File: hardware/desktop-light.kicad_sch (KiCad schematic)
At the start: 54 parts

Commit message: led position
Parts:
- added D55, D56, D57, D58, D59, D60: WS2812B, LED_SMD:LED_WS2812B_PLCC4_5.0x5.0mm_P3.2mm, symbol LED:WS2812B
- added J1, J2: Conn_01x06, Connector_JST:JST_SH_BM06B-SRSS-TB_1x06-1MP_P1.00mm_Vertical, symbol Connector_Generic:Conn_01x06
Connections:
- net +5V: now also D55.1 (VDD), D56.1 (VDD), D57.1 (VDD), D58.1 (VDD), D59.1 (VDD), D60.1 (VDD), J1.1 (Pin_1), J1.2 (Pin_2), J2.5 (Pin_5), J2.6 (Pin_6)
- net GND: now also D55.3 (VSS), D56.3 (VSS), D57.3 (VSS), D58.3 (VSS), D59.3 (VSS), D60.3 (VSS), J1.5 (Pin_5), J1.6 (Pin_6), J2.1 (Pin_1), J2.2 (Pin_2)
- net at D54.2 (DOUT): now also D55.4 (DIN)
- net at D1.4 (DIN): now also J1.3 (Pin_3)
- new net: D55.2 (DOUT), D56.4 (DIN)
- new net: D59.2 (DOUT), D60.4 (DIN)
- new net: D58.2 (DOUT), D59.4 (DIN)
- new net: D56.2 (DOUT), D57.4 (DIN)
- new net: D57.2 (DOUT), D58.4 (DIN)
- new net DIN: J2.4 (Pin_4)
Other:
- moved on the sheet: D1, D10, D11, D12, D13, D14, D15, D16, D17, D18, D19, D2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

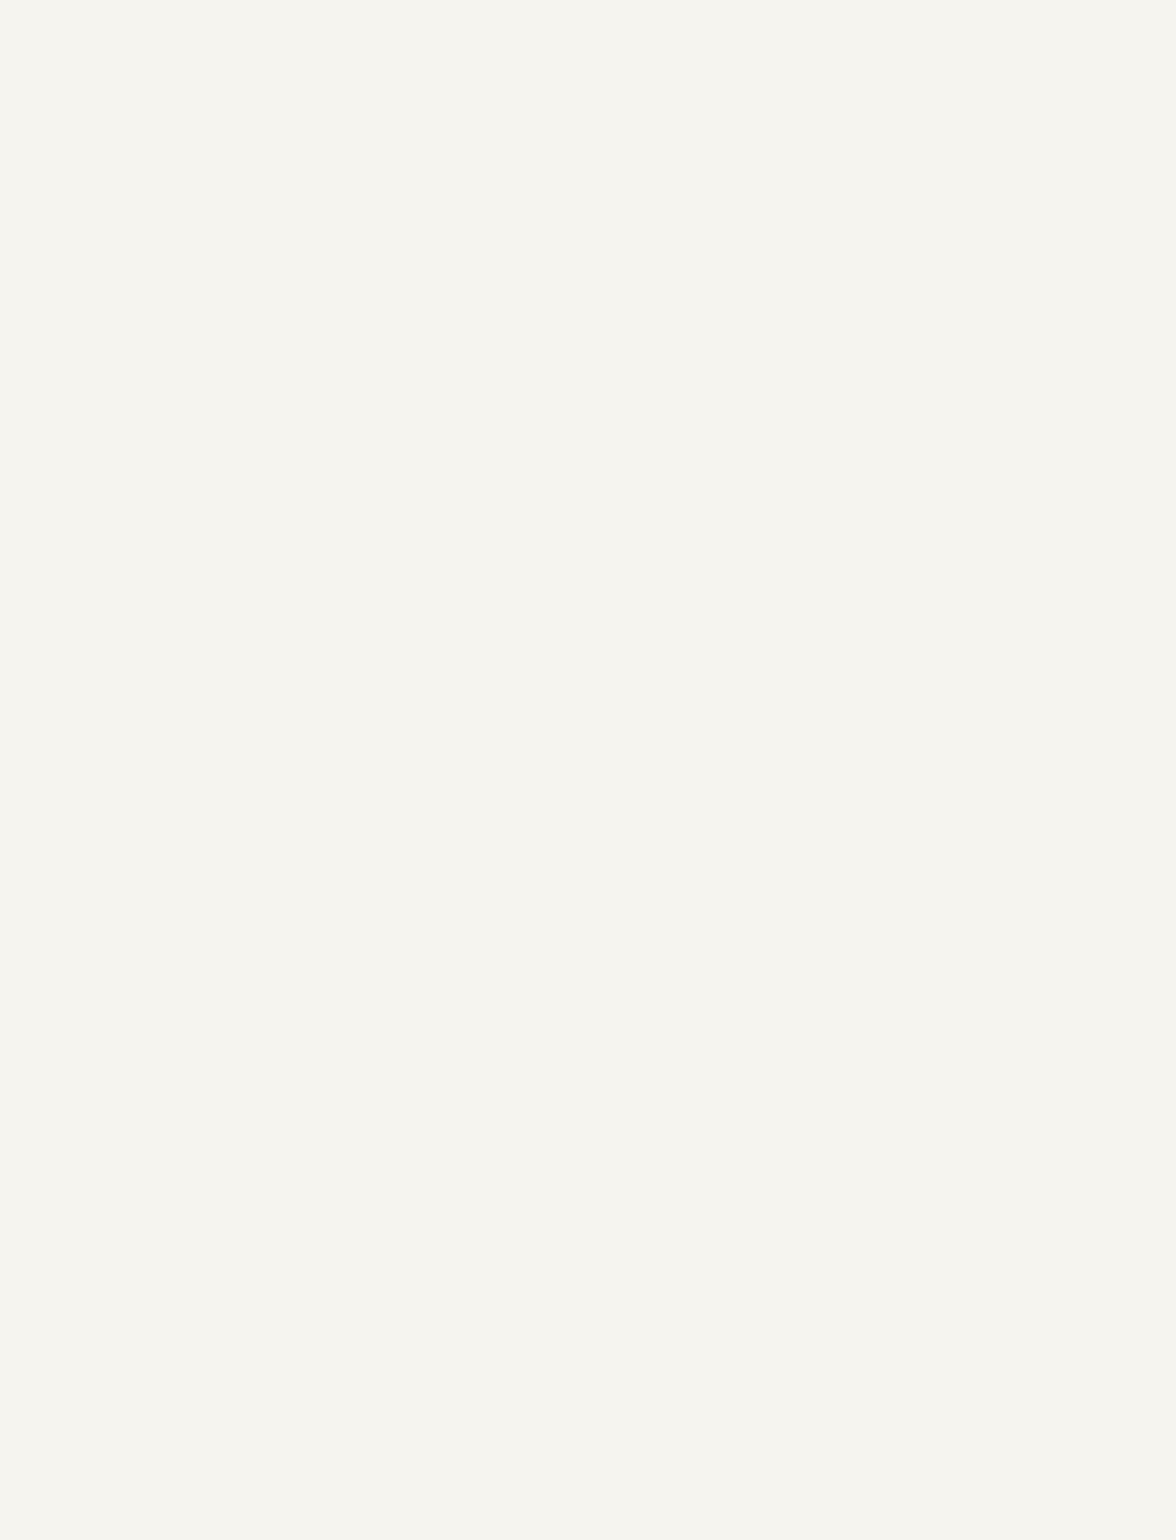
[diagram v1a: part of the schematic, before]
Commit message: add esp32
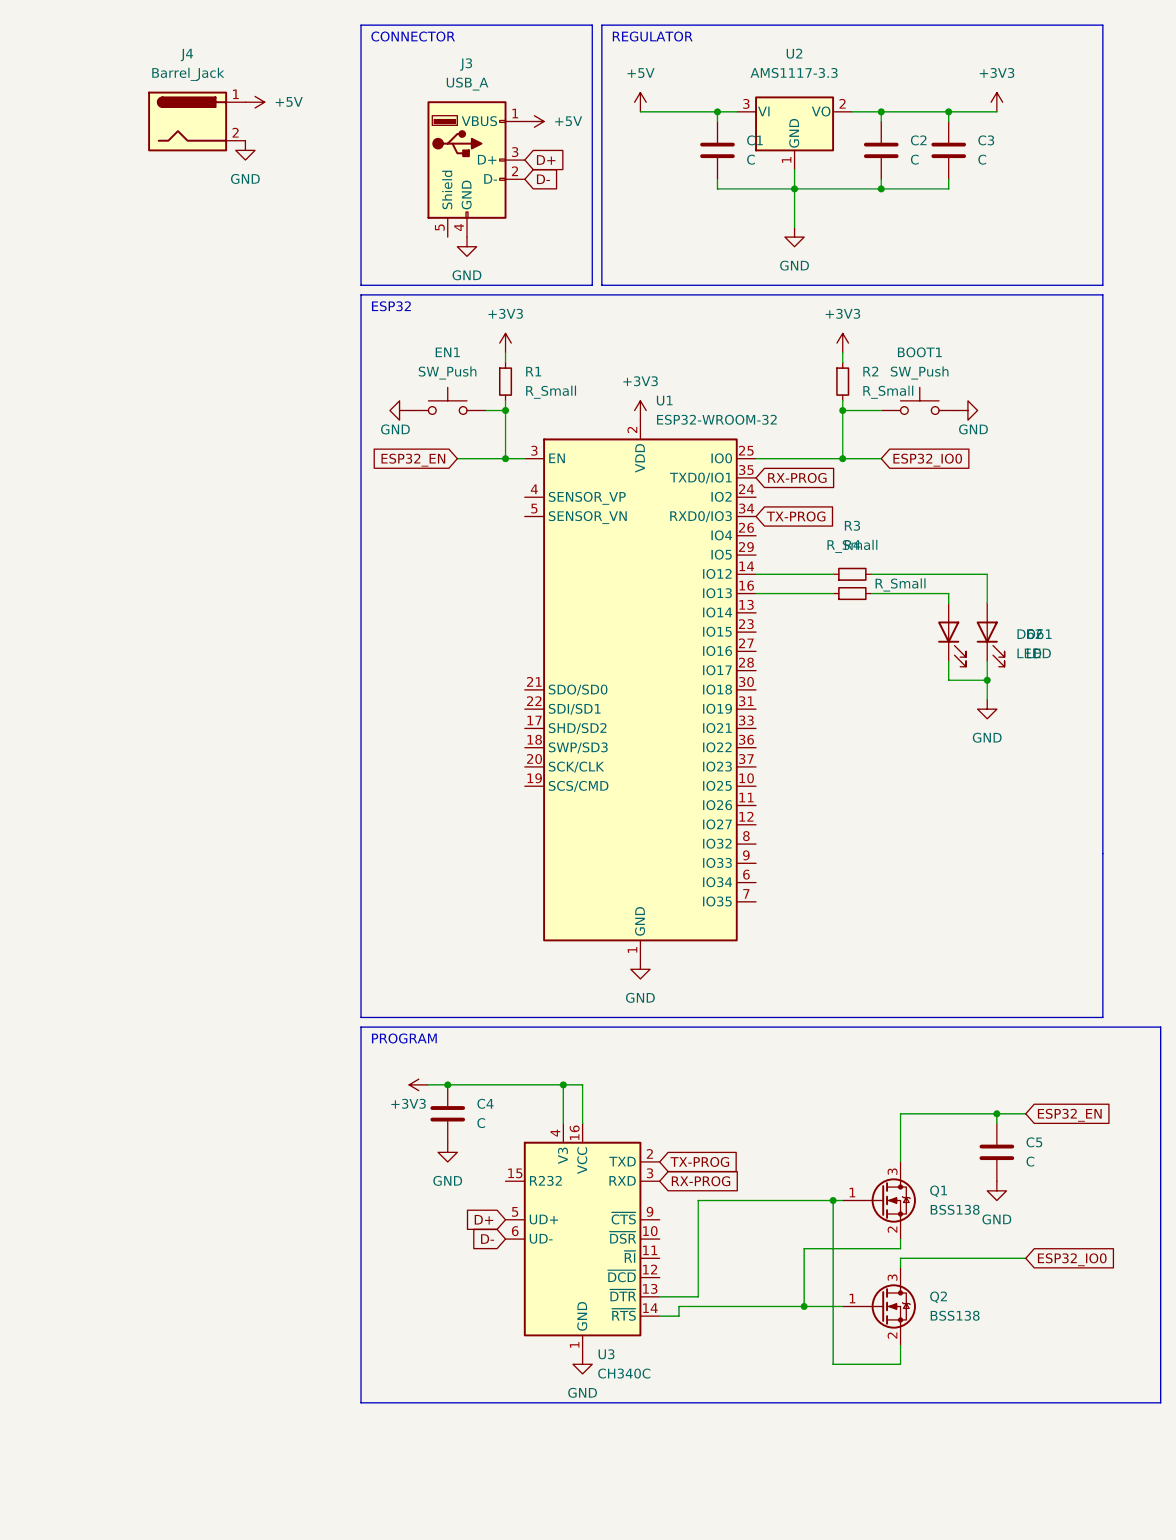
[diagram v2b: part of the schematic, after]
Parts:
- added BOOT1, EN1: SW_Push, Button_Switch_SMD:SW_SPST_FSMSM, symbol Switch:SW_Push
- added C1, C2, C3, C4, C5: C, Capacitor_SMD:C_0603_1608Metric, symbol Device:C
- added D61, D62: LED, LED_SMD:LED_0603_1608Metric, symbol Device:LED
- added J3: USB_A, Connector_USB:USB_A_CNCTech_1001-011-01101_Horizontal, symbol Connector:USB_A
- added J4: Barrel_Jack, symbol Connector:Barrel_Jack
- added Q1, Q2: BSS138, Package_TO_SOT_SMD:SOT-23, symbol Transistor_FET:BSS138
- added R1, R2, R3, R4: R_Small, Resistor_SMD:R_0603_1608Metric, symbol Device:R_Small
- added U1: ESP32-WROOM-32, RF_Module:ESP32-WROOM-32, symbol RF_Module:ESP32-WROOM-32
- added U2: AMS1117-3.3, Package_TO_SOT_SMD:SOT-223-3_TabPin2, symbol Regulator_Linear:AMS1117-3.3
- added U3: CH340C, Package_SO:SOIC-16_3.9x9.9mm_P1.27mm, symbol Interface_USB:CH340C
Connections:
- net +5V: now also C1.1, J3.1 (VBUS), J4.1, U2.3 (VI)
- net GND: now also BOOT1.2, C1.2, C2.2, C3.2, C4.2, C5.2, D61.1 (K), D62.1 (K), EN1.1, J3.4 (GND), J4.2, U1.1 (GND), U1.15 (GND), U1.38 (GND), U1.39 (GND), U2.1 (GND), U3.1 (GND)
- new net: Q1.1 (G), Q2.2 (S), U3.13 (~{DTR})
- new net: Q1.2 (S), Q2.1 (G), U3.14 (~{RTS})
- new net: R4.1, U1.16 (IO13)
- new net: D61.2 (A), R4.2
- new net: R3.1, U1.14 (IO12)
- new net: D62.2 (A), R3.2
- new net +3V3: C2.1, C3.1, C4.1, R1.1, R2.1, U1.2 (VDD), U2.2 (VO), U3.16 (VCC), U3.4 (V3)
- new net D+: J3.3 (D+), U3.5 (UD+)
- new net D-: J3.2 (D-), U3.6 (UD-)
- new net ESP32_EN: C5.1, EN1.2, Q1.3 (D), R1.2, U1.3 (EN)
- new net ESP32_IO0: BOOT1.1, Q2.3 (D), R2.2, U1.25 (IO0)
- new net RX-PROG: U1.35 (TXD0/IO1), U3.3 (RXD)
- new net TX-PROG: U1.34 (RXD0/IO3), U3.2 (TXD)
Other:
- note added: "CONNECTOR"
- note added: "ESP32"
- note added: "PROGRAM"
- note added: "REGULATOR"

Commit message: add clock
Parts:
- removed J3: USB_A, Connector_USB:USB_A_CNCTech_1001-011-01101_Horizontal, symbol Connector:USB_A
- added BT1: Battery_Cell, Battery:BatteryHolder_LINX_BAT-HLD-012-SMT, symbol Device:Battery_Cell
- added BTN1, BTN2, BTN3: SW_Push, Button_Switch_SMD:SW_SPST_FSMSM, symbol Switch:SW_Push
- added C6: C_Small, Capacitor_SMD:C_0603_1608Metric, symbol Device:C_Small
- added J3: USB_B_Micro, Connector_USB:USB_Micro-B_Molex-105017-0001, symbol Connector:USB_B_Micro
- added R5, R6, R7, R8, R9: R_Small, Resistor_SMD:R_0603_1608Metric, symbol Device:R_Small
- added U4: PCF8523T, Package_SO:SOIC-8_3.9x4.9mm_P1.27mm, symbol Timer_RTC:PCF8523T
- added Y1: ABS2532768KHZ6T, Crystal:Crystal_SMD_Abracon_ABS25-4Pin_8.0x3.8mm, symbol ABS2532768KHZ6T:ABS2532768KHZ6T
- J4: footprint (none) -> Connector_BarrelJack:BarrelJack_Wuerth_6941xx301002
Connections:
- net +3V3: now also R7.1, R8.1, R9.1
- net +5V: now also J3.1 (VBUS)
- net D+: now also J3.3 (D+)
- net D-: now also J3.2 (D-)
- net GND: now also BT1.2 (-), BTN1.2, BTN2.2, BTN3.2, C6.2, J3.5 (GND), U4.4 (VSS)
- net BTN1: now reaches U1.13 (IO14)
- net BTN1: now also BTN1.1, R7.2
- net BTN2: now reaches U1.23 (IO15)
- net BTN2: now also BTN2.1, R8.2
- net BTN3: now reaches U1.27 (IO16)
- net BTN3: now also BTN3.1, R9.2
- net SDA: now reaches U1.33 (IO21)
- net SDA: now also R5.2, U4.5 (SDA)
- net SCL: now reaches U1.36 (IO22)
- net SCL: now also R6.2, U4.6 (SCL)
- new net: U4.1 (OSCI), Y1.1
- new net: Y1.2 (NC), Y1.3 (NC)
- new net: U4.2 (OSCO), Y1.4
- new net: BT1.1 (+), U4.3 (VBAT)
- new net VCC: C6.1, R5.1, R6.1, U4.8 (VDD)
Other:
- note added: "RTC PCF8523"
- moved on the sheet: J2

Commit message: finish wiring
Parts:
- added J5: Conn_01x06, Connector_JST:JST_SH_BM06B-SRSS-TB_1x06-1MP_P1.00mm_Vertical, symbol Connector_Generic:Conn_01x06
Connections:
- net VCC is gone; now on net +3V3: C6.1, R5.1, R6.1, U4.8 (VDD)
- net +5V: now also J5.1 (Pin_1), J5.2 (Pin_2)
- net GND: now also J5.5 (Pin_5), J5.6 (Pin_6)
- net at D60.2 (DOUT): now also J5.3 (Pin_3)

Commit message: add real photos
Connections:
- net DIN: now also U1.28 (IO17)
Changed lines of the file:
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@@
+		)
+	)
+	(global_label "DIN"
+		(shape input)
+		(at 351.79 100.33 0)
+		(fields_autoplaced yes)
+		(effects
+			(font
+				(size 1.27 1.27)
+			)
+			(justify left)
+		)
+		(property "Intersheetrefs" "${INTERSHEET_REFS}"
+			(at 357.9805 100.33 0)
+			(effects
+				(font
+					(size 1.27 1.27)
+				)
+				(justify left)
+				(hide yes)
+			)
 		)
 	)
